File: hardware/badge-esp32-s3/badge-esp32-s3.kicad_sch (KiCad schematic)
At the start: 4 parts, among them U1 ESP32-S3-WROOM-1(N16R8)

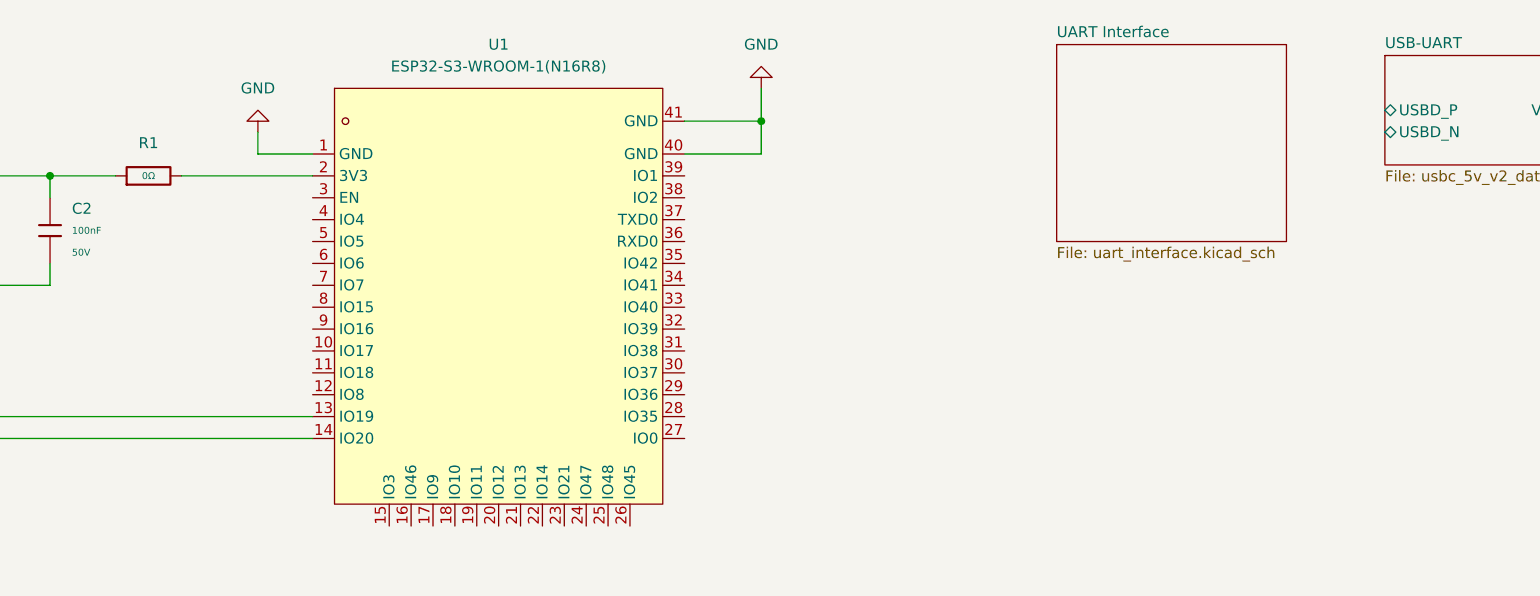
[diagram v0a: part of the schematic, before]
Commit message: Finish USB-UART subcircuit
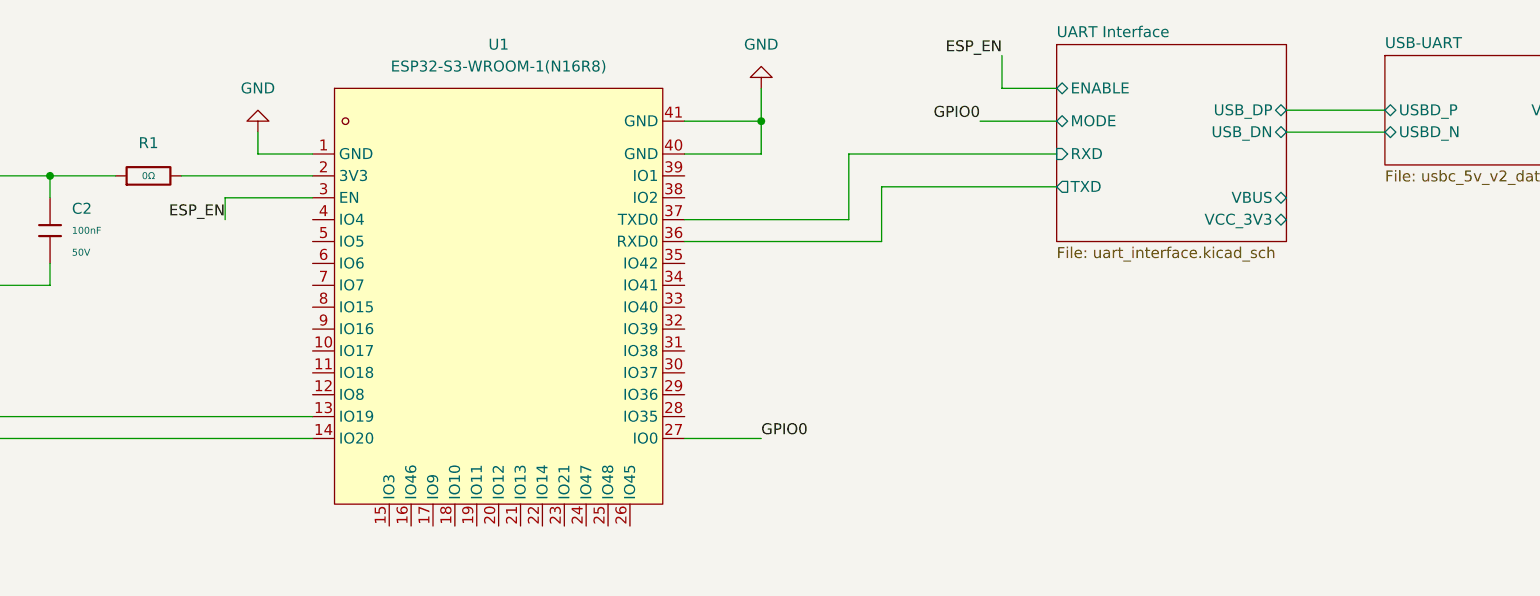
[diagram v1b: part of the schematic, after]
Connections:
- net GPIO0: now reaches U1.27 (IO0)
- net ESP_EN: now reaches U1.3 (EN)
- net UART Interface/TXD: now reaches U1.36 (RXD0)
- net UART Interface/RXD: now reaches U1.37 (TXD0)
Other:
- sheet UART Interface ports: added ENABLE, MODE, RXD, TXD, USB_DN, USB_DP, VBUS, VCC_3V3; removed none
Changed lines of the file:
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@@
+	(wire
+		(pts
+			(xy 187.96 38.1) (xy 187.96 31.75)
+		)
+		(stroke
+			(width 0)
+			(type default)
+		)
+	)
 	(wire
 		(pts
@@
 	(wire
 		(pts
+			(xy 234.95 22.86) (xy 246.38 22.86)
+		)
+		(stroke
+			(width 0)
+			(type default)
+		)
+	)
+	(wire
+		(pts
 			(xy 115.57 25.4) (xy 115.57 27.94)
 		)
@@
 	(wire
 		(pts
+			(xy 234.95 25.4) (xy 246.38 25.4)
+		)
+		(stroke
+			(width 0)
+			(type default)
+		)
+	)
+	(wire
+		(pts
 			(xy 78.74 43.18) (xy 78.74 48.26)
 		)
@@
 	(wire
 		(pts
+			(xy 199.39 24.13) (xy 208.28 24.13)
+		)
+		(stroke
+			(width 0)
+			(type default)
+		)
+	)
+	(wire
+		(pts
 			(xy 91.44 30.48) (xy 91.44 33.02)
 		)
@@
 	(wire
 		(pts
+			(xy 201.93 20.32) (xy 208.28 20.32)
+		)
+		(stroke
+			(width 0)
+			(type default)
+		)
+	)
+	(wire
+		(pts
 			(xy 71.12 58.42) (xy 71.12 49.53)
 		)
@@
 	(wire
 		(pts
+			(xy 165.1 35.56) (xy 184.15 35.56)
+		)
+		(stroke
+			(width 0)
+			(type default)
+		)
+	)
+	(wire
+		(pts
 			(xy 50.8 76.2) (xy 57.15 76.2)
 		)
@@
 	(wire
 		(pts
+			(xy 165.1 60.96) (xy 173.99 60.96)
+		)
+		(stroke
+			(width 0)
+			(type default)
+		)
+	)
+	(wire
+		(pts
 			(xy 121.92 27.94) (xy 115.57 27.94)
 		)
@@
 	(wire
 		(pts
+			(xy 184.15 27.94) (xy 208.28 27.94)
+		)
+		(stroke
+			(width 0)
+			(type default)
+		)
+	)
+	(wire
+		(pts
 			(xy 78.74 30.48) (xy 91.44 30.48)
 		)
@@
 	(wire
 		(pts
+			(xy 187.96 31.75) (xy 208.28 31.75)
+		)
+		(stroke
+			(width 0)
+			(type default)
+		)
+	)
+	(wire
+		(pts
 			(xy 276.86 25.4) (xy 271.78 25.4)
 		)
@@
 	(wire
 		(pts
+			(xy 165.1 38.1) (xy 187.96 38.1)
+		)
+		(stroke
+			(width 0)
+			(type default)
+		)
+	)
+	(wire
+		(pts
 			(xy 20.32 49.53) (xy 25.4 49.53)
 		)
@@
 	(wire
 		(pts
+			(xy 111.76 33.02) (xy 121.92 33.02)
+		)
+		(stroke
+			(width 0)
+			(type default)
+		)
+	)
+	(wire
+		(pts
 			(xy 165.1 24.13) (xy 173.99 24.13)
 		)
@@
 	(wire
 		(pts
+			(xy 111.76 35.56) (xy 111.76 33.02)
+		)
+		(stroke
+			(width 0)
+			(type default)
+		)
+	)
+	(wire
+		(pts
 			(xy 78.74 30.48) (xy 78.74 33.02)
 		)
@@
 	(wire
 		(pts
+			(xy 201.93 16.51) (xy 201.93 20.32)
+		)
+		(stroke
+			(width 0)
+			(type default)
+		)
+	)
+	(wire
+		(pts
 			(xy 165.1 27.94) (xy 173.99 27.94)
 		)
@@
 			(width 0)
 			(type default)
+		)
+	)
+	(wire
+		(pts
+			(xy 184.15 35.56) (xy 184.15 27.94)
+		)
+		(stroke
+			(width 0)
+			(type default)
+		)
+	)
+	(label "ESP_EN"
+		(at 201.93 16.51 180)
+		(effects
+			(font
+				(size 1.27 1.27)
+			)
+			(justify right bottom)
 		)
 	)
@@
 		)
 	)
+	(label "GPIO0"
+		(at 199.39 24.13 180)
+		(effects
+			(font
+				(size 1.27 1.27)
+			)
+			(justify right bottom)
+		)
+	)
+	(label "GPIO0"
+		(at 173.99 60.96 0)
+		(effects
+			(font
+				(size 1.27 1.27)
+			)
+			(justify left bottom)
+		)
+	)
 	(label "VBUS"
 		(at 276.86 25.4 0)
@@
 	(label "VCC_5V"
 		(at 20.32 52.07 180)
+		(effects
+			(font
+				(size 1.27 1.27)
+			)
+			(justify right bottom)
+		)
+	)
+	(label "ESP_EN"
+		(at 111.76 35.56 180)
 		(effects
 			(font
@@
 			)
 		)
+		(pin "ENABLE" bidirectional
+			(at 208.28 20.32 180)
+			(effects
+				(font
+					(size 1.27 1.27)
+				)
+				(justify left)
+			)
+		)
+		(pin "MODE" bidirectional
+			(at 208.28 24.13 180)
+			(effects
+				(font
+					(size 1.27 1.27)
+				)
+				(justify left)
+			)
+		)
+		(pin "RXD" input
+			(at 208.28 27.94 180)
+			(effects
+				(font
+					(size 1.27 1.27)
+				)
+				(justify left)
+			)
+		)
+		(pin "TXD" output
+			(at 208.28 31.75 180)
+			(effects
+				(font
+					(size 1.27 1.27)
+				)
+				(justify left)
+			)
+		)
+		(pin "USB_DN" bidirectional
+			(at 234.95 25.4 0)
+			(effects
+				(font
+					(size 1.27 1.27)
+				)
+				(justify right)
+			)
+		)
+		(pin "USB_DP" bidirectional
+			(at 234.95 22.86 0)
+			(effects
+				(font
+					(size 1.27 1.27)
+				)
+				(justify right)
+			)
+		)
+		(pin "VBUS" bidirectional
+			(at 234.95 33.02 0)
+			(effects
+				(font
+					(size 1.27 1.27)
+				)
+				(justify right)
+			)
+		)
+		(pin "VCC_3V3" bidirectional
+			(at 234.95 35.56 0)
+			(effects
+				(font
+					(size 1.27 1.27)
+				)
+				(justify right)
+			)
+		)

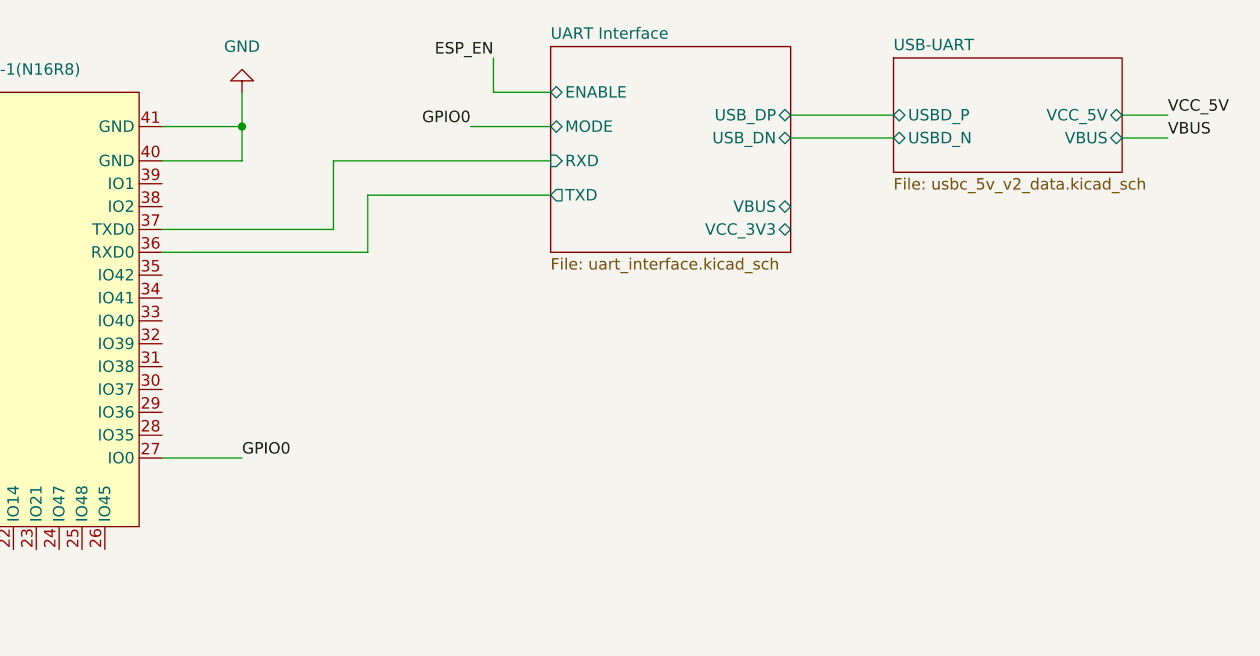
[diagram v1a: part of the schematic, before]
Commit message: Schematic on par with basic devkit
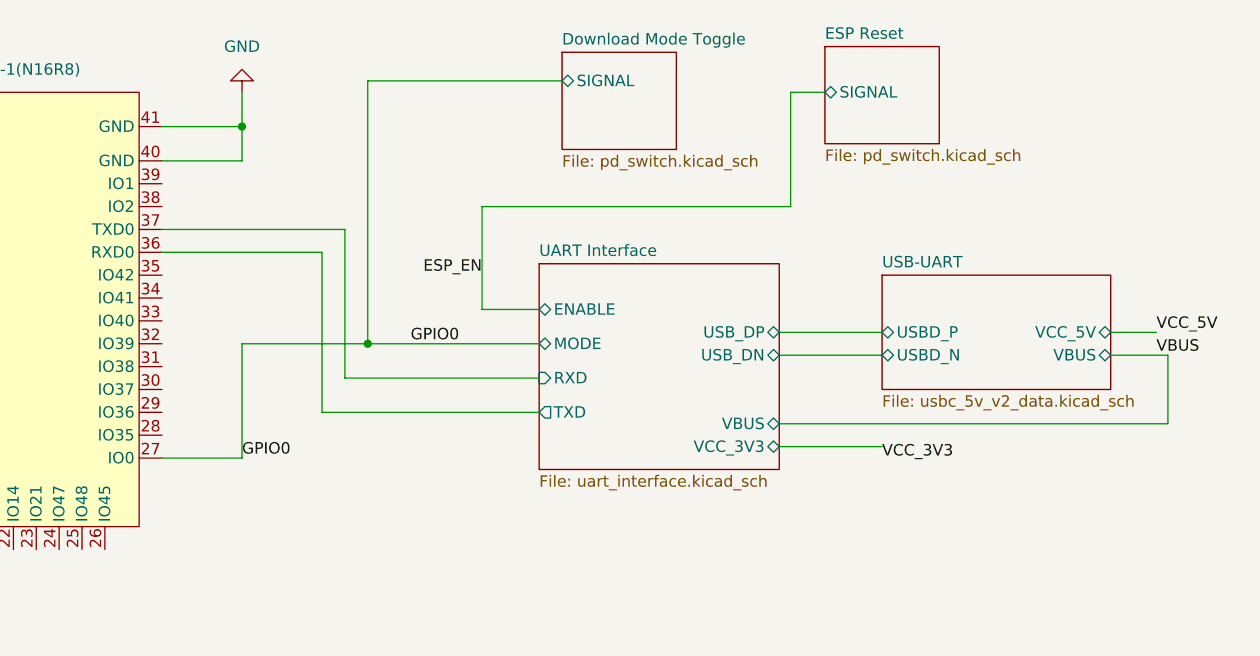
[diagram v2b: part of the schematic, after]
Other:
- added sheet Download Mode Toggle (pd_switch.kicad_sch)
- added sheet ESP Reset (pd_switch.kicad_sch)

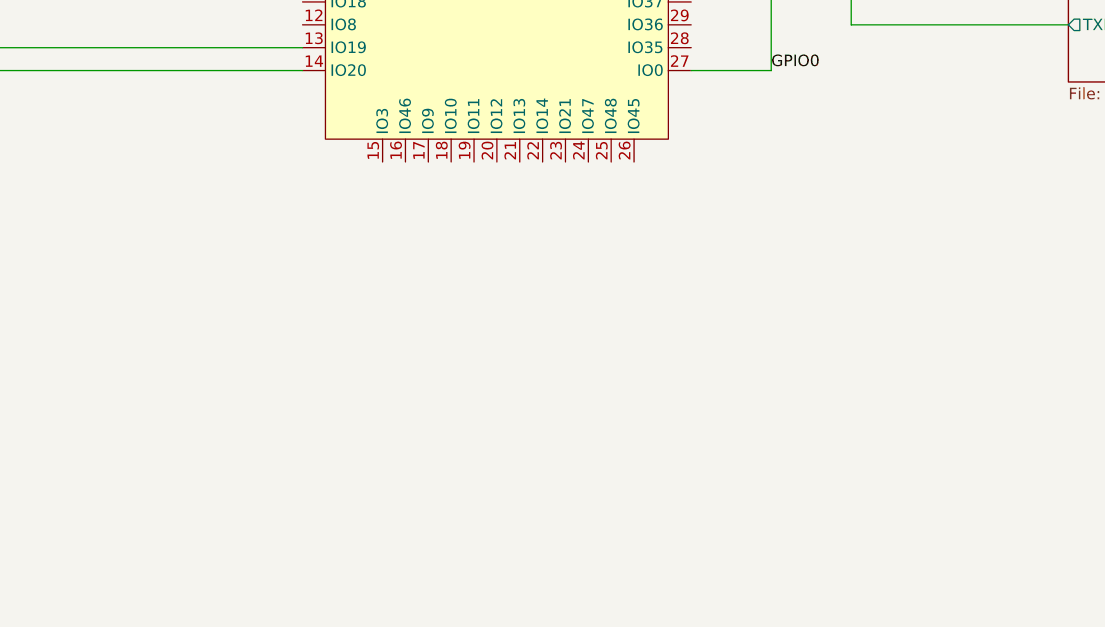
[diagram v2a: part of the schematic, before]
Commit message: add display block
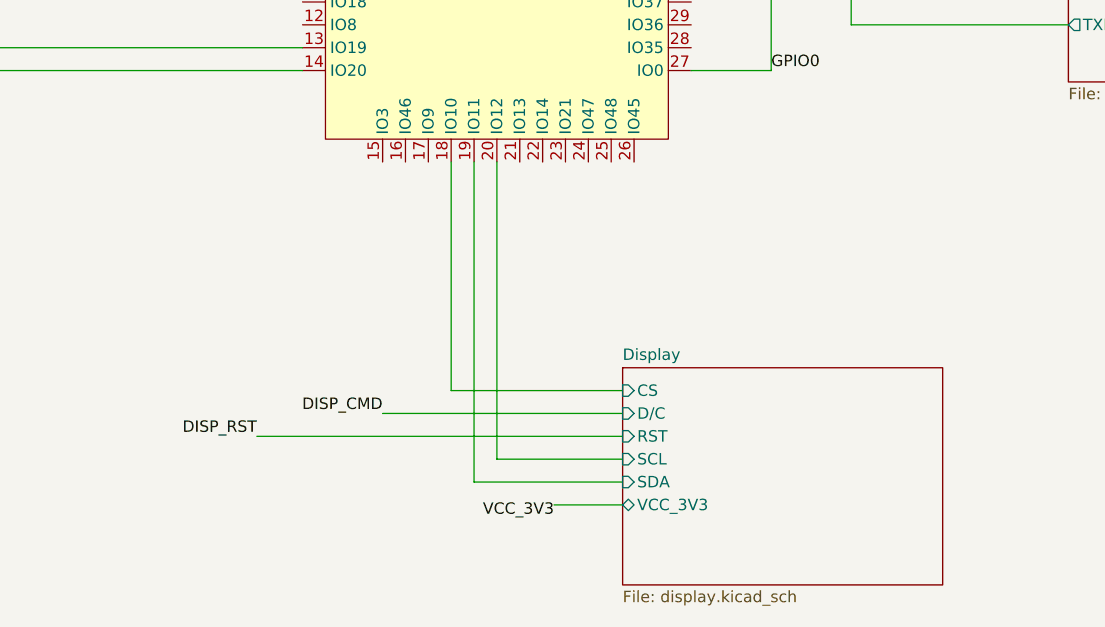
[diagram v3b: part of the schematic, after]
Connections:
- net Display/CS: now reaches U1.18 (IO10)
- net Display/SDA: now reaches U1.19 (IO11)
- net Display/SCL: now reaches U1.20 (IO12)
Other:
- added sheet Display (display.kicad_sch)
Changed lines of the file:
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@@
+	(wire
+		(pts
+			(xy 149.86 109.22) (xy 157.48 109.22)
+		)
+		(stroke
+			(width 0)
+			(type default)
+		)
+	)
 	(wire
 		(pts
@@
 	(wire
 		(pts
+			(xy 140.97 106.68) (xy 157.48 106.68)
+		)
+		(stroke
+			(width 0)
+			(type default)
+		)
+	)
+	(wire
+		(pts
 			(xy 91.44 43.18) (xy 78.74 43.18)
 		)
@@
 	(wire
 		(pts
+			(xy 143.51 71.12) (xy 143.51 104.14)
+		)
+		(stroke
+			(width 0)
+			(type default)
+		)
+	)
+	(wire
+		(pts
+			(xy 138.43 71.12) (xy 138.43 96.52)
+		)
+		(stroke
+			(width 0)
+			(type default)
+		)
+	)
+	(wire
+		(pts
 			(xy 165.1 60.96) (xy 173.99 60.96)
 		)
@@
 	(wire
 		(pts
+			(xy 143.51 104.14) (xy 157.48 104.14)
+		)
+		(stroke
+			(width 0)
+			(type default)
+		)
+	)
+	(wire
+		(pts
 			(xy 173.99 48.26) (xy 173.99 60.96)
 		)
@@
 	(wire
 		(pts
+			(xy 130.81 99.06) (xy 157.48 99.06)
+		)
+		(stroke
+			(width 0)
+			(type default)
+		)
+	)
+	(wire
+		(pts
 			(xy 71.12 49.53) (xy 50.8 49.53)
 		)
@@
 	(wire
 		(pts
+			(xy 116.84 101.6) (xy 157.48 101.6)
+		)
+		(stroke
+			(width 0)
+			(type default)
+		)
+	)
+	(wire
+		(pts
+			(xy 138.43 96.52) (xy 157.48 96.52)
+		)
+		(stroke
+			(width 0)
+			(type default)
+		)
+	)
+	(wire
+		(pts
 			(xy 78.74 30.48) (xy 91.44 30.48)
 		)
@@
 		(pts
 			(xy 185.42 52.07) (xy 185.42 35.56)
+		)
+		(stroke
+			(width 0)
+			(type default)
+		)
+	)
+	(wire
+		(pts
+			(xy 140.97 71.12) (xy 140.97 106.68)
 		)
 		(stroke
@@
 		)
 	)
+	(label "DISP_CMD"
+		(at 130.81 99.06 180)
+		(effects
+			(font
+				(size 1.27 1.27)
+			)
+			(justify right bottom)
+		)
+	)
 	(label "GPIO0"
 		(at 198.12 48.26 180)
@@
 		)
 	)
+	(label "VCC_3V3"
+		(at 149.86 109.22 180)
+		(effects
+			(font
+				(size 1.27 1.27)
+			)
+			(justify right top)
+		)
+	)
 	(label "VCC_5V"
 		(at 275.59 46.99 0)
@@
 	(label "ESP_EN"
 		(at 111.76 35.56 180)
+		(effects
+			(font
+				(size 1.27 1.27)
+			)
+			(justify right bottom)
+		)
+	)
+	(label "DISP_RST"
+		(at 116.84 101.6 180)
 		(effects
 			(font
@@
 				)
 			)
+		)
+	)
+	(sheet
+		(at 157.48 93.98)
+		(size 35.56 24.13)
+		(exclude_from_sim no)
+		(in_bom yes)
+		(on_board yes)
+		(dnp no)
+		(fields_autoplaced yes)
+		(stroke
+			(width 0.1524)
+			(type solid)
+		)
+		(fill
+			(color 0 0 0 0.0000)
+		)
+		(property "Sheetname" "Display"
+			(at 157.48 93.2684 0)
+			(effects
+				(font
+					(size 1.27 1.27)
+				)
+				(justify left bottom)
+			)
+		)
+		(property "Sheetfile" "display.kicad_sch"
+			(at 157.48 118.6946 0)
+			(effects
+				(font
+					(size 1.27 1.27)
+				)
+				(justify left top)
+			)
+		)
+		(pin "CS" input
+			(at 157.48 96.52 180)
+			(effects
+				(font
+					(size 1.27 1.27)
+				)
+				(justify left)
+			)
+		)
+		(pin "D{slash}C" input
+			(at 157.48 99.06 180)
+			(effects
+				(font
+					(size 1.27 1.27)
+				)
+				(justify left)
+			)
+		)
+		(pin "RST" input
+			(at 157.48 101.6 180)
+			(effects
+				(font
+					(size 1.27 1.27)
+				)
+				(justify left)
+			)
+		)
+		(pin "SCL" input
+			(at 157.48 104.14 180)
+			(effects
+				(font
+					(size 1.27 1.27)
+				)
+				(justify left)
+			)
+		)
+		(pin "SDA" input
+			(at 157.48 106.68 180)
+			(effects
+				(font
+					(size 1.27 1.27)
+				)
+				(justify left)
+			)
+		)
+		(pin "VCC_3V3" bidirectional
+			(at 157.48 109.22 180)
+			(effects
+				(font
+					(size 1.27 1.27)
+				)
+				(justify left)
+			)
+		)
+		(instances
+			(project "badge-esp32-s3"
+				(path "/e2af9a6c-dbe9-4de2-9ba6-ea213a7300ec"
+					(page "8")
+				)
+			)

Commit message: Add some gamepad generic stuff
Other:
- added sheet Gamepad (gamepad.kicad_sch)
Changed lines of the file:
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@@
+	)
+	(sheet
+		(at 210.185 93.345)
+		(size 18.415 15.875)
+		(exclude_from_sim no)
+		(in_bom yes)
+		(on_board yes)
+		(dnp no)
+		(fields_autoplaced yes)
+		(stroke
+			(width 0.1524)
+			(type solid)
+		)
+		(fill
+			(color 0 0 0 0.0000)
+		)
+		(property "Sheetname" "Gamepad"
+			(at 210.185 92.6334 0)
+			(effects
+				(font
+					(size 1.27 1.27)
+				)
+				(justify left bottom)
+			)
+		)
+		(property "Sheetfile" "gamepad.kicad_sch"
+			(at 210.185 109.8046 0)
+			(effects
+				(font
+					(size 1.27 1.27)
+				)
+				(justify left top)
+			)
+		)
+		(instances
+			(project "badge-esp32-s3"
+				(path "/e2af9a6c-dbe9-4de2-9ba6-ea213a7300ec"
+					(page "9")
+				)
+			)
+		)
 	)
 	(sheet
